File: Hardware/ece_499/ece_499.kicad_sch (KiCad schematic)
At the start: 44 parts, among them J1 Conn_01x04, J2 Conn_01x04, J3 Conn_01x04, J4 Conn_01x04, J5 Conn_01x04, Q1 DMN2004WK, Q2 DMN2004WK, Q3 DMN2004WK, Q4 DMN2004WK, SW1 RotaryEncoder_Switch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

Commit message: Set up PEC16 footprint
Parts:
- SW1: footprint (none) -> Imported_Parts:PEC16-4015F-S0024
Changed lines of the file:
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@@
       (effects (font (size 1.27 1.27)))
     )
-    (property "Footprint" "" (at 30.48 73.406 0)
+    (property "Footprint" "Imported_Parts:PEC16-4015F-S0024" (at 30.48 73.406 0)
       (effects (font (size 1.27 1.27)) hide)
     )
-    (property "Datasheet" "~" (at 34.29 70.866 0)
+    (property "Datasheet" "https://www.bourns.com/docs/Product-Datasheets/pec16.pdf" (at 34.29 70.866 0)
       (effects (font (size 1.27 1.27)) hide)
     )

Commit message: Validate footprints(corrected B5817W)
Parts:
- D1: footprint Diode_THT:D_DO-41_SOD81_P10.16mm_Horizontal -> Diode_SMD:D_SOD-123
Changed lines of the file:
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@@
       (effects (font (size 1.27 1.27)))
     )
-    (property "Footprint" "Diode_THT:D_DO-41_SOD81_P10.16mm_Horizontal" (at 77.47 47.625 0)
+    (property "Footprint" "Diode_SMD:D_SOD-123" (at 77.47 47.625 0)
       (effects (font (size 1.27 1.27)) hide)
     )
-    (property "Datasheet" "http://www.vishay.com/docs/88525/1n5817.pdf" (at 77.47 43.18 0)
+    (property "Datasheet" "https://www.smc-diodes.com/propdf/B5817W-B5819W%20N1752%20REV.-.pdf" (at 77.47 43.18 0)
       (effects (font (size 1.27 1.27)) hide)
     )

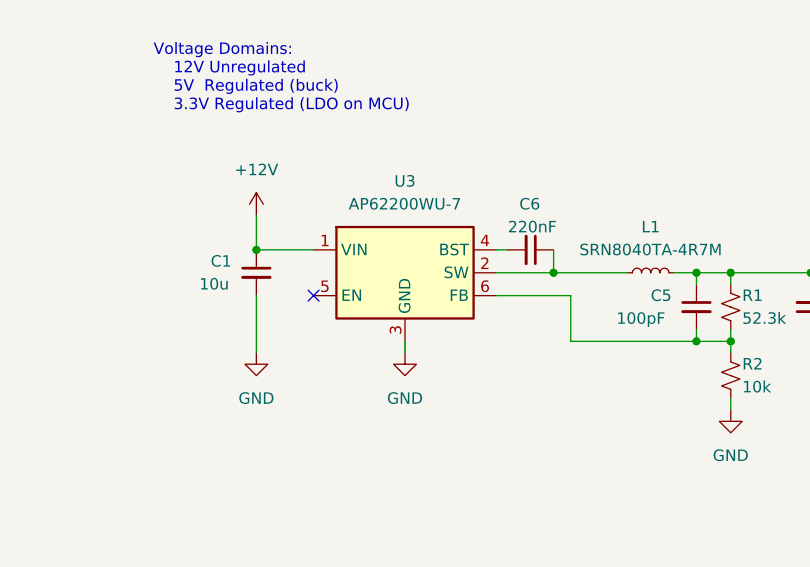
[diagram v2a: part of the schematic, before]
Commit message: Initial PCB layout and fix reg schema
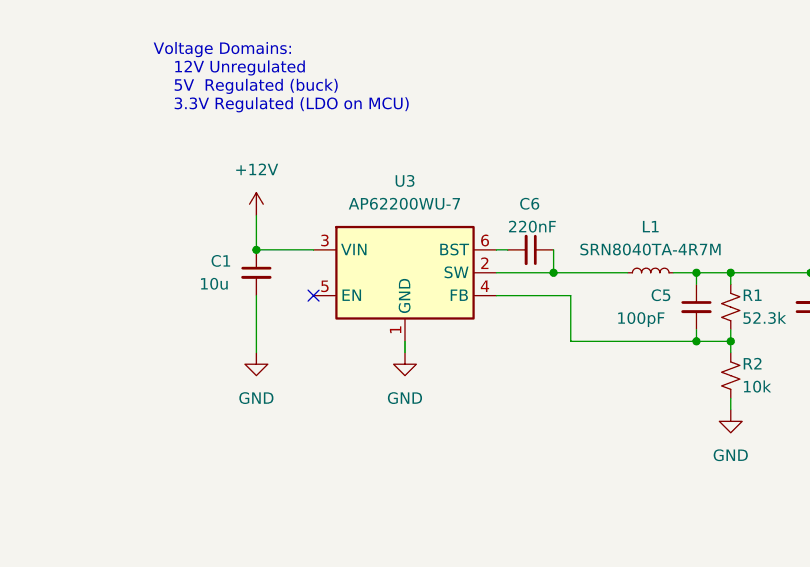
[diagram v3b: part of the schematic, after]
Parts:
- U3: footprint Package_TO_SOT_SMD:SOT-563 -> Package_TO_SOT_SMD:SOT-23-6_Handsoldering
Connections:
- net +12V: now also U3.3 (VIN); no longer U3.1 (VIN)
- net GND: now also U3.1 (GND); no longer U3.3 (GND)
- net at C5.2, R1.2, R2.1: now also U3.4 (FB); no longer U3.6 (FB)
- net at C6.2: now also U3.6 (BST); no longer U3.4 (BST)
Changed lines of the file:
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@@
       (effects (font (size 1.27 1.27)))
     )
-    (property "Footprint" "Package_TO_SOT_SMD:SOT-563" (at 209.55 35.56 0)
+    (property "Footprint" "Package_TO_SOT_SMD:SOT-23-6_Handsoldering" (at 209.55 35.56 0)
       (effects (font (size 1.27 1.27)) hide)
     )
-    (property "Datasheet" "https://www.diodes.com/assets/Datasheets/AP62250.pdf" (at 209.55 33.02 0)
+    (property "Datasheet" "https://www.diodes.com/assets/Datasheets/AP62200_AP62201_AP62200T.pdf" (at 209.55 33.02 0)
       (effects (font (size 1.27 1.27)) hide)
     )

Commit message: Cursed debouncy :(
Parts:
- removed R3, R4, R5: 10k, Resistor_SMD:R_1206_3216Metric_Pad1.30x1.75mm_HandSolder, symbol Device:R_Small_US
- added C4, C7, C8: 22u, Capacitor_SMD:C_0805_2012Metric_Pad1.18x1.45mm_HandSolder, symbol Device:C_Small
- added D6, D7, D8: B5817W, Diode_SMD:D_SOD-123, symbol Diode:1N5817
- added JP1, JP2, JP3: SolderJumper_2_Open, symbol Jumper:SolderJumper_2_Open
- added JP4, JP5, JP6: SolderJumper_2_Bridged, symbol Jumper:SolderJumper_2_Bridged
- added R10, R12, R4: 3.3k, symbol Device:R_US
- added R11, R3, R5: 2.7k, symbol Device:R_US
- added U5: CD74HC14M96, Package_SO:SO-14_3.9x8.65mm_P1.27mm, symbol Imported_Parts:CD74HC14M96
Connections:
- net +3V3: now also R11.1, R3.1, R5.1, U5.14 (Vcc)
- net GND: now also SW1.S2, C4.2, C7.2, C8.2, U5.11 (5A), U5.13 (6A), U5.7 (GND), U5.9 (4A)
- net at SW1.A: now also D6.2 (A), JP1.1 (A), R3.2, R4.2
- net encoder_A: now reaches U1.7 (TX_D6)
- net encoder_A: now also JP1.2 (B), JP4.2 (B)
- net at SW1.S1: now also D8.2 (A), JP2.1 (A), R11.2, R12.2
- net encoder_sw: now reaches U1.13 (D8)
- net encoder_sw: now also JP2.2 (B), JP5.2 (B); no longer SW1.S2
- net encoder_B: now reaches U1.14 (RX_D7)
- net encoder_B: now also JP3.2 (B), JP6.2 (B)
- net at SW1.B: now also D7.2 (A), JP3.1 (A), R10.2, R5.2
- new net: JP4.1 (A), U5.2 (1Y)
- new net: JP5.1 (A), U5.4 (2Y)
- new net: C7.1, D6.1 (K), R4.1, U5.1 (1A)
- new net: C8.1, D8.1 (K), R12.1, U5.3 (2A)
- new net: C4.1, D7.1 (K), R10.1, U5.5 (3A)
- new net: JP6.1 (A), U5.6 (3Y)
- no-connect marks 5 -> 8
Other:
- note removed: "Debounce in software or hardware?"
- moved on the sheet: D1, J1, J2, J3, J4, J5, Q1, Q2, Q3, Q4, SW1, U1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

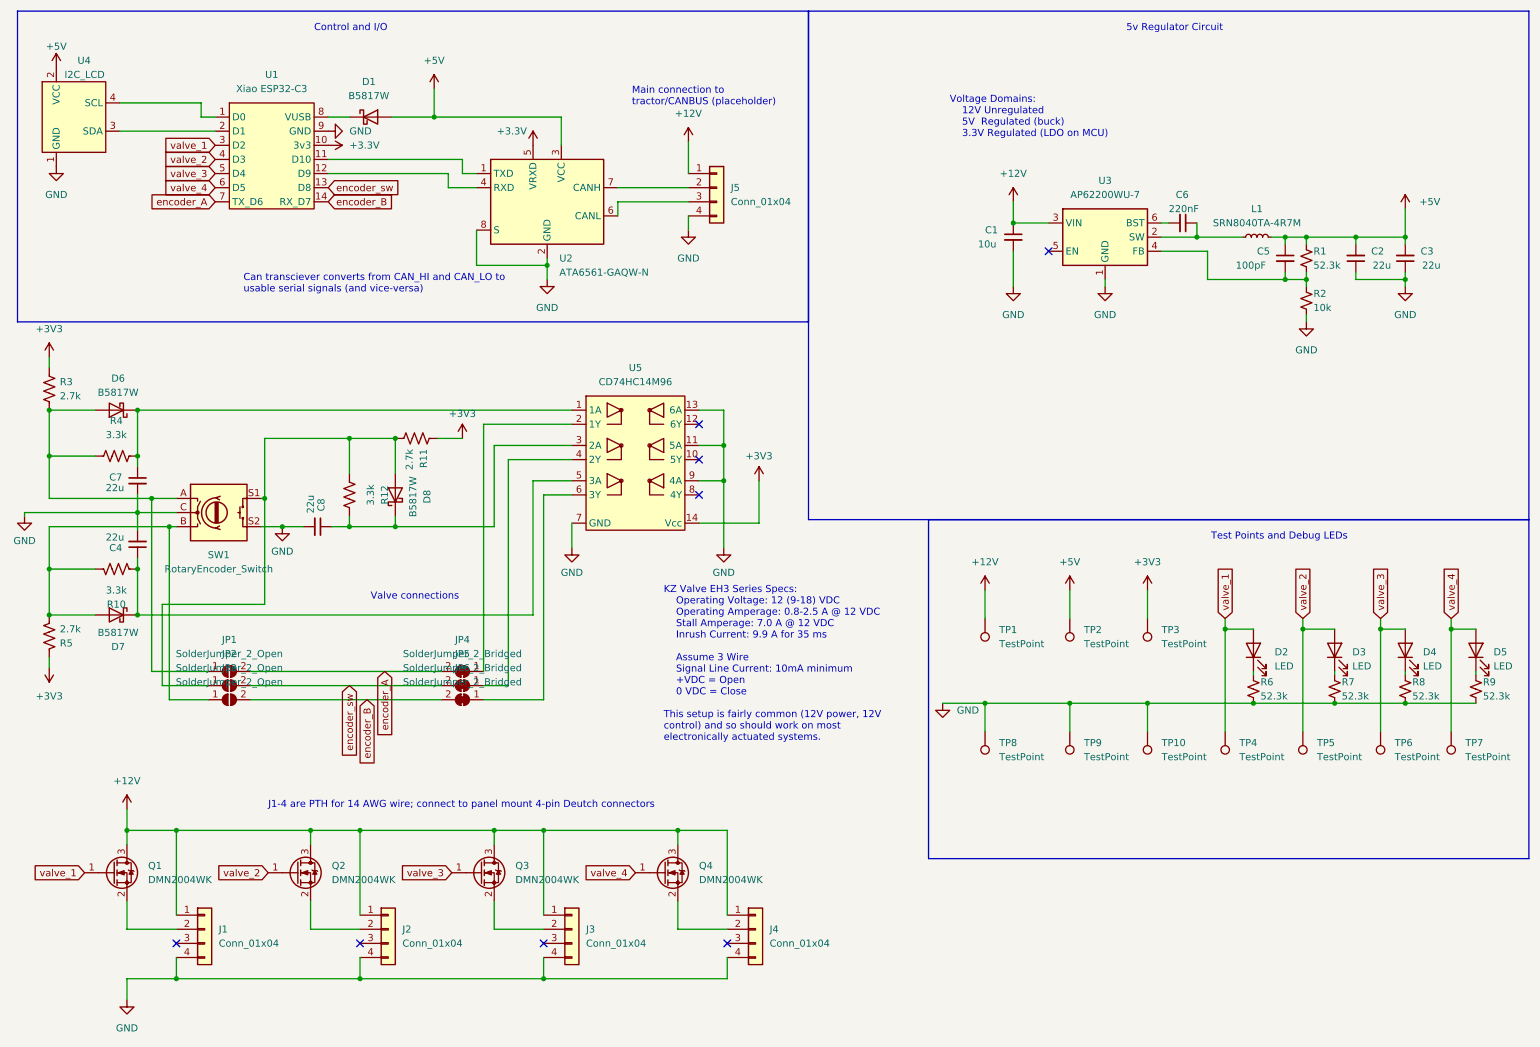
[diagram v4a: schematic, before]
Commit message: Fix (?) debounce schema
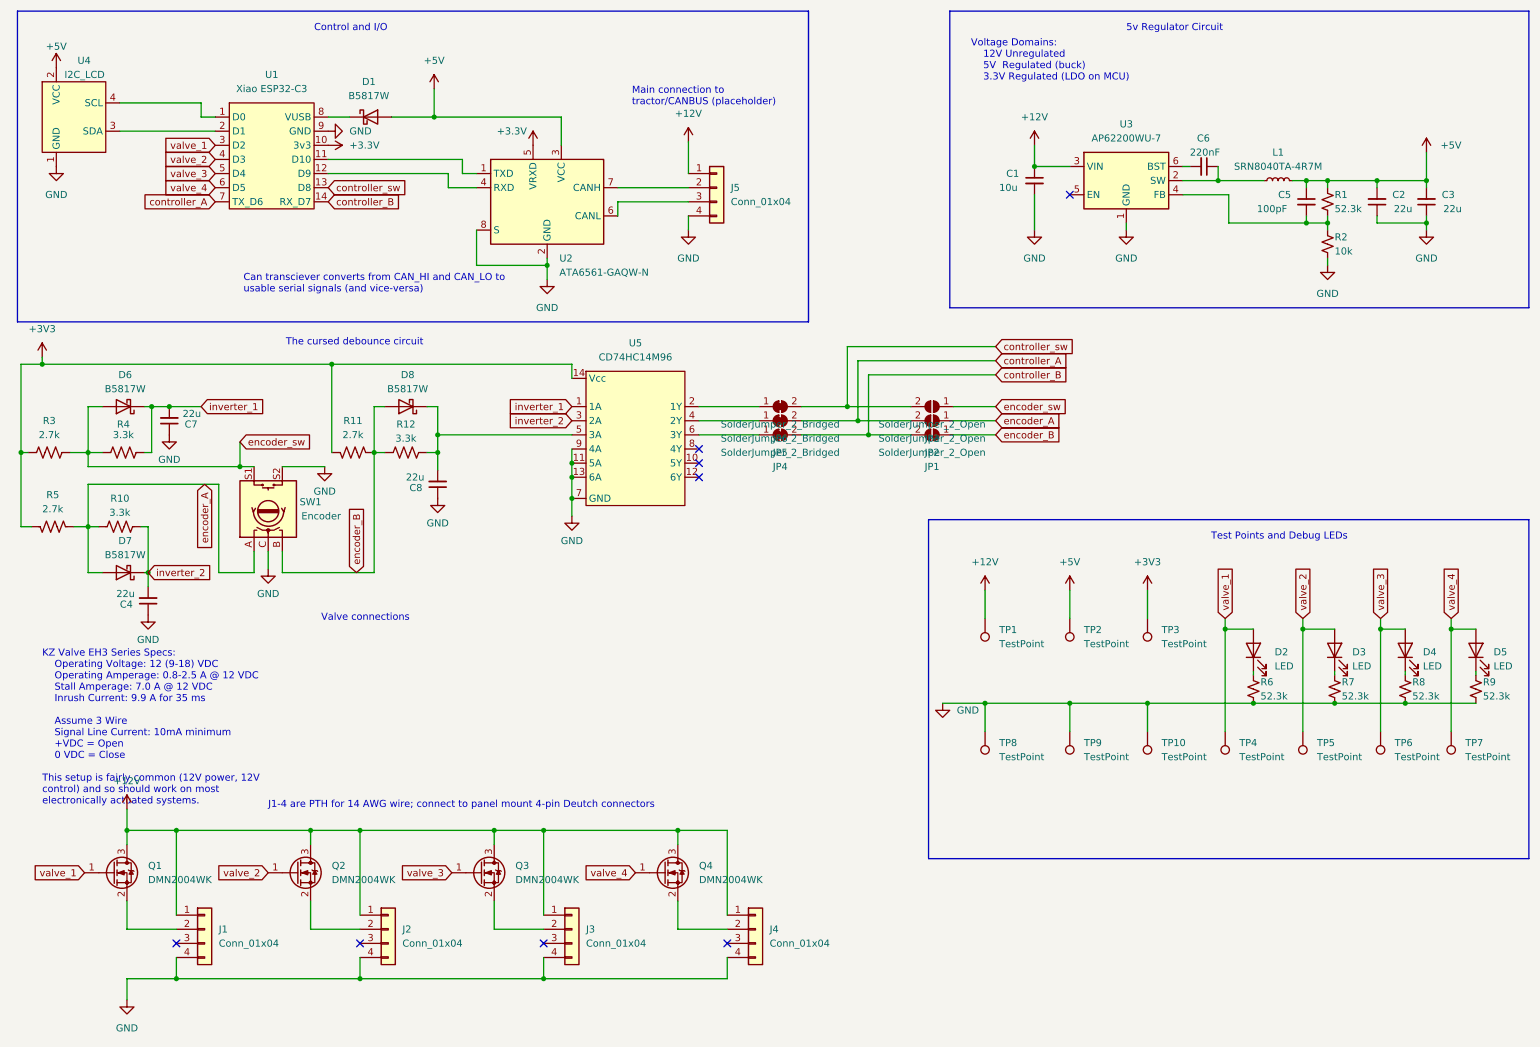
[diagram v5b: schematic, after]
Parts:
- SW1: value RotaryEncoder_Switch -> Encoder
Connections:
- net GND: now also C4.1, C7.1, C8.1; no longer C4.2, C7.2, C8.2
- net encoder_A: now also D7.2 (A), JP2.1 (A), R10.2, R5.2, SW1.A; no longer JP1.2 (B), JP4.2 (B), U1.7 (TX_D6)
- net encoder_B: now also D8.2 (A), JP1.1 (A), R11.2, R12.2, SW1.B; no longer JP3.2 (B), JP6.2 (B), U1.14 (RX_D7)
- net encoder_sw: now also D6.2 (A), JP3.1 (A), R3.2, R4.2, SW1.S1; no longer JP2.2 (B), JP5.2 (B), U1.13 (D8)
- net at JP4.1 (A): now also U5.6 (3Y); no longer U5.2 (1Y)
- net inverter_1: now reaches D6.1 (K), R4.1, U5.1 (1A)
- net inverter_1: now also C7.2; no longer C7.1
- net at D8.1 (K), R12.1: now also C8.2, U5.5 (3A); no longer C8.1, U5.3 (2A)
- net inverter_2: now reaches D7.1 (K), R10.1
- net inverter_2: now also C4.2, U5.3 (2A); no longer C4.1, U5.5 (3A)
- net at JP6.1 (A): now also U5.2 (1Y); no longer U5.6 (3Y)
- new net controller_A: JP2.2 (B), JP5.2 (B), U1.7 (TX_D6)
- new net controller_B: JP1.2 (B), JP4.2 (B), U1.14 (RX_D7)
- new net controller_sw: JP3.2 (B), JP6.2 (B), U1.13 (D8)
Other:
- note added: "The cursed debounce circuit"
- moved on the sheet: C1, C2, C3, C4, C5, C6, C7, D6, D7, JP1, JP2, JP3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

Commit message: Add new encoder design to initial PCB layout
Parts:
- JP1, JP2, JP3: footprint (none) -> Jumper:SolderJumper-2_P1.3mm_Open_RoundedPad1.0x1.5mm
- JP4, JP5, JP6: footprint (none) -> Jumper:SolderJumper-2_P1.3mm_Bridged2Bar_RoundedPad1.0x1.5mm
- R10, R11, R12, R3, R4, R5: footprint (none) -> Resistor_SMD:R_1206_3216Metric_Pad1.30x1.75mm_HandSolder
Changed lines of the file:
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@@
       (effects (font (size 1.27 1.27)))
     )
-    (property "Footprint" "" (at 149.86 88.9 0)
+    (property "Footprint" "Jumper:SolderJumper-2_P1.3mm_Bridged2Bar_RoundedPad1.0x1.5mm" (at 149.86 88.9 0)
       (effects (font (size 1.27 1.27)) hide)
     )
@@
       (effects (font (size 1.27 1.27)))
     )
-    (property "Footprint" "" (at 149.86 86.36 0)
+    (property "Footprint" "Jumper:SolderJumper-2_P1.3mm_Bridged2Bar_RoundedPad1.0x1.5mm" (at 149.86 86.36 0)
       (effects (font (size 1.27 1.27)) hide)
     )
@@
       (effects (font (size 1.27 1.27)))
     )
-    (property "Footprint" "" (at 19.304 106.426 90)
+    (property "Footprint" "Resistor_SMD:R_1206_3216Metric_Pad1.30x1.75mm_HandSolder" (at 19.304 106.426 90)
       (effects (font (size 1.27 1.27)) hide)
     )
@@
       (effects (font (size 1.27 1.27)))
     )
-    (property "Footprint" "" (at 73.279 93.091 90)
+    (property "Footprint" "Resistor_SMD:R_1206_3216Metric_Pad1.30x1.75mm_HandSolder" (at 73.279 93.091 90)
       (effects (font (size 1.27 1.27)) hide)
     )
@@
       (effects (font (size 1.27 1.27)))
     )
-    (property "Footprint" "" (at 177.165 88.9 0)
+    (property "Footprint" "Jumper:SolderJumper-2_P1.3mm_Open_RoundedPad1.0x1.5mm" (at 177.165 88.9 0)
       (effects (font (size 1.27 1.27)) hide)
     )
@@
       (effects (font (size 1.27 1.27)))
     )
-    (property "Footprint" "" (at 149.86 83.82 0)
+    (property "Footprint" "Jumper:SolderJumper-2_P1.3mm_Bridged2Bar_RoundedPad1.0x1.5mm" (at 149.86 83.82 0)
       (effects (font (size 1.27 1.27)) hide)
     )
@@
       (effects (font (size 1.27 1.27)))
     )
-    (property "Footprint" "" (at 31.496 93.091 90)
+    (property "Footprint" "Resistor_SMD:R_1206_3216Metric_Pad1.30x1.75mm_HandSolder" (at 31.496 93.091 90)
       (effects (font (size 1.27 1.27)) hide)
     )
@@
       (effects (font (size 1.27 1.27)))
     )
-    (property "Footprint" "" (at 18.669 91.059 90)
+    (property "Footprint" "Resistor_SMD:R_1206_3216Metric_Pad1.30x1.75mm_HandSolder" (at 18.669 91.059 90)
       (effects (font (size 1.27 1.27)) hide)
     )
@@
       (effects (font (size 1.27 1.27)))
     )
-    (property "Footprint" "" (at 177.165 83.82 0)
+    (property "Footprint" "Jumper:SolderJumper-2_P1.3mm_Open_RoundedPad1.0x1.5mm" (at 177.165 83.82 0)
       (effects (font (size 1.27 1.27)) hide)
     )
@@
       (effects (font (size 1.27 1.27)))
     )
-    (property "Footprint" "" (at 82.296 93.091 90)
+    (property "Footprint" "Resistor_SMD:R_1206_3216Metric_Pad1.30x1.75mm_HandSolder" (at 82.296 93.091 90)
       (effects (font (size 1.27 1.27)) hide)
     )
@@
       (effects (font (size 1.27 1.27)))
     )
-    (property "Footprint" "" (at 30.861 106.426 90)
+    (property "Footprint" "Resistor_SMD:R_1206_3216Metric_Pad1.30x1.75mm_HandSolder" (at 30.861 106.426 90)
       (effects (font (size 1.27 1.27)) hide)
     )
@@
       (effects (font (size 1.27 1.27)))
     )
-    (property "Footprint" "" (at 177.165 86.36 0)
-      (effects (font (size 1.27 1.27)) hide)
-    )
+    (property "Footprint" "Jumper:SolderJumper-2_P1.3mm_Open_RoundedPad1.0x1.5mm" (at 177.165 86.36 0)
+      (effects (font (size 1.27 1.27)) hide)
+    )

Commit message: Implement 3v3 lines on PCB
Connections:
- net +3.3V is gone; now on net +3V3: U1.10 (3v3), U2.5 (VRXD)
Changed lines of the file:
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@@
   (junction (at 107.95 58.42) (diameter 0) (color 0 0 0 0)
+  )
+  (junction (at 95.885 36.83) (diameter 0) (color 0 0 0 0)
   )
   (junction (at 17.145 76.2) (diameter 0) (color 0 0 0 0)
@@
     (stroke (width 0) (type default))
   )
+  (wire (pts (xy 95.885 26.035) (xy 95.885 36.83))
+    (stroke (width 0) (type default))
+  )
   (wire (pts (xy 212.09 52.07) (xy 212.09 50.8))
     (stroke (width 0) (type default))
@@
     (stroke (width 0) (type default))
   )
+  (wire (pts (xy 95.885 36.83) (xy 105.41 36.83))
+    (stroke (width 0) (type default))
+  )
   (wire (pts (xy 74.295 186.69) (xy 107.315 186.69))
     (stroke (width 0) (type default))
@@
   )
   (wire (pts (xy 74.295 186.69) (xy 74.295 182.88))
+    (stroke (width 0) (type default))
+  )
+  (wire (pts (xy 68.58 36.83) (xy 95.885 36.83))
     (stroke (width 0) (type default))
   )
@@
         (path "/3f2f140e-ca1f-4768-bf63-ce27bfebd1d1"
           (reference "C7") (unit 1)
-        )
-      )
-    )
-  )
-  (symbol (lib_id "power:+3.3V") (at 68.58 36.83 270) (unit 1)
-    (in_bom yes) (on_board yes) (dnp no) (fields_autoplaced)
-    (property "Reference" "#PWR010" (at 64.77 36.83 0)
-      (effects (font (size 1.27 1.27)) hide)
-    )
-    (property "Value" "+3.3V" (at 72.39 36.83 90)
-      (effects (font (size 1.27 1.27)) (justify left))
-    )
-    (property "Footprint" "" (at 68.58 36.83 0)
-      (effects (font (size 1.27 1.27)) hide)
-    )
-    (property "Datasheet" "" (at 68.58 36.83 0)
-      (effects (font (size 1.27 1.27)) hide)
-    )
-    (pin "1")
-    (instances
-      (project "ece_499"
-        (path "/3f2f140e-ca1f-4768-bf63-ce27bfebd1d1"
-          (reference "#PWR010") (unit 1)
         )
       )
@@
     )
   )
-  (symbol (lib_id "power:+3.3V") (at 105.41 36.83 0) (unit 1)
-    (in_bom yes) (on_board yes) (dnp no)
-    (property "Reference" "#PWR015" (at 105.41 40.64 0)
-      (effects (font (size 1.27 1.27)) hide)
-    )
-    (property "Value" "+3.3V" (at 101.6 34.29 0)
-      (effects (font (size 1.27 1.27)))
-    )
-    (property "Footprint" "" (at 105.41 36.83 0)
-      (effects (font (size 1.27 1.27)) hide)
-    )
-    (property "Datasheet" "" (at 105.41 36.83 0)
-      (effects (font (size 1.27 1.27)) hide)
-    )
-    (pin "1")
-    (instances
-      (project "ece_499"
-        (path "/3f2f140e-ca1f-4768-bf63-ce27bfebd1d1"
-          (reference "#PWR015") (unit 1)
-        )
-      )
-    )
-  )
   (symbol (lib_id "Connector_Generic:Conn_01x04") (at 112.395 177.8 0) (unit 1)
     (in_bom yes) (on_board yes) (dnp no) (fields_autoplaced)
@@
         )
       )
+    )
+  )
+  (symbol (lib_id "power:+3V3") (at 95.885 26.035 0) (unit 1)
+    (in_bom yes) (on_board yes) (dnp no) (fields_autoplaced)
+    (property "Reference" "#PWR010" (at 95.885 29.845 0)
+      (effects (font (size 1.27 1.27)) hide)
+    )
+    (property "Value" "+3V3" (at 95.885 21.59 0)
+      (effects (font (size 1.27 1.27)))
+    )
+    (property "Footprint" "" (at 95.885 26.035 0)
+      (effects (font (size 1.27 1.27)) hide)
+    )
+    (property "Datasheet" "" (at 95.885 26.035 0)
+      (effects (font (size 1.27 1.27)) hide)
+    )
+    (pin "1")
+    (instances
+      (project "ece_499"
+        (path "/3f2f140e-ca1f-4768-bf63-ce27bfebd1d1"
+          (reference "#PWR010") (unit 1)
+        )
+      )
